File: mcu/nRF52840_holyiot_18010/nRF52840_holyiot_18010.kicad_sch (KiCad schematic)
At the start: 3 parts

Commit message: add reset module
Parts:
- removed MCU_SW1: SW_Push, ErgoCai.pretty:K2-1187SQ, symbol Switch:SW_Push
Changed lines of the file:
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@@
-		)
-	)
-	(wire
-		(pts
-			(xy 143.51 54.61) (xy 144.78 54.61)
-		)
-		(stroke
-			(width 0)
-			(type solid)
 		)
 	)
@@
 		(property "Intersheetrefs" "${INTERSHEET_REFS}"
 			(at 90.17 97.6303 90)
-			(effects
-				(font
-					(size 1.27 1.27)
-				)
-				(justify right)
-				(hide yes)
-			)
-		)
-	)
-	(global_label "RESET"
-		(shape input)
-		(at 143.51 54.61 180)
-		(fields_autoplaced yes)
-		(effects
-			(font
-				(size 1.27 1.27)
-			)
-			(justify right)
-		)
-		(property "Intersheetrefs" "${INTERSHEET_REFS}"
-			(at 134.7797 54.61 0)
 			(effects
 				(font
@@
 					(unit 1)
 				)
-			)
-		)
-	)
-	(symbol
-		(lib_id "power:GND")
-		(at 154.94 54.61 90)
-		(unit 1)
-		(exclude_from_sim no)
-		(in_bom yes)
-		(on_board yes)
-		(dnp no)
-		(property "Reference" "#PWR0103"
-			(at 161.29 54.61 0)
-			(effects
-				(font
-					(size 1.27 1.27)
-				)
-				(hide yes)
-			)
-		)
-		(property "Value" "GND"
-			(at 158.75 54.61 0)
-			(effects
-				(font
-					(size 1.27 1.27)
-				)
-			)
-		)
-		(property "Footprint" ""
-			(at 154.94 54.61 0)
-			(effects
-				(font
-					(size 1.27 1.27)
-				)
-				(hide yes)
-			)
-		)
-		(property "Datasheet" ""
-			(at 154.94 54.61 0)
-			(effects
-				(font
-					(size 1.27 1.27)
-				)
-				(hide yes)
-			)
-		)
-		(property "Description" "Power symbol creates a global label with name \"GND\" , ground"
-			(at 154.94 54.61 0)
-			(effects
-				(font
-					(size 1.27 1.27)
-				)
-				(hide yes)
-			)
-		)
-		(pin "1"
-		)
-		(instances
-			(project "nRF52840_holyiot_18010"
-				(path "/a75e1a70-312e-4b3d-9ad5-017ab62e82c1"
-					(reference "#PWR0103")
-					(unit 1)
-				)
-			)
-		)
-	)
-	(symbol
-		(lib_id "Switch:SW_Push")
-		(at 149.86 54.61 0)
-		(unit 1)
-		(exclude_from_sim no)
-		(in_bom yes)
-		(on_board yes)
-		(dnp no)
-		(property "Reference" "MCU_SW1"
-			(at 149.86 47.625 0)
-			(effects
-				(font
-					(size 1.27 1.27)
-				)
-			)
-		)
-		(property "Value" "SW_Push"
-			(at 149.86 50.165 0)
-			(effects
-				(font
-					(size 1.27 1.27)
-				)
-			)
-		)
-		(property "Footprint" "ErgoCai.pretty:K2-1187SQ"
-			(at 149.86 49.53 0)
-			(effects
-				(font
-					(size 1.27 1.27)
-				)
-				(hide yes)
-			)
-		)
-		(property "Datasheet" "~"
-			(at 149.86 49.53 0)
-			(effects
-				(font
-					(size 1.27 1.27)
-				)
-				(hide yes)
-			)
-		)
-		(property "Description" "Push button switch, generic, two pins"
-			(at 149.86 54.61 0)
-			(effects
-				(font
-					(size 1.27 1.27)
-				)
-				(hide yes)
-			)
-		)
-		(pin "1"
-		)
-		(pin "2"
-		)
-		(instances
-			(project "nRF52840_holyiot_18010"
-				(path "/a75e1a70-312e-4b3d-9ad5-017ab62e82c1"
-					(reference "MCU_SW1")
-					(unit 1)
-				)

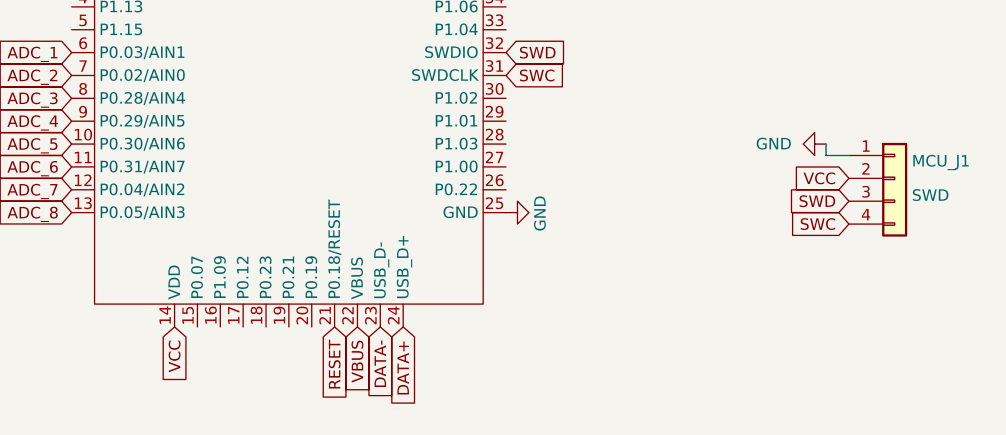
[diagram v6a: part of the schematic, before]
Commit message: update to 3.3V tag
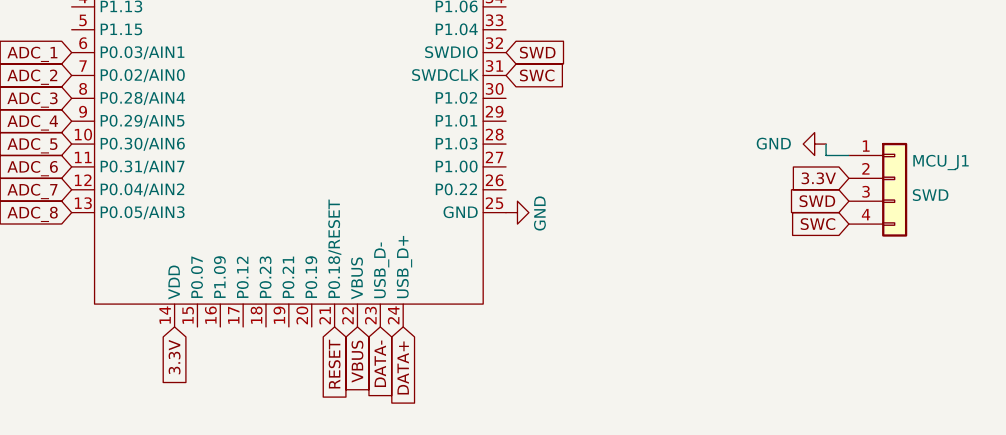
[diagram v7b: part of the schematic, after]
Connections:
- net VCC renamed 3.3V
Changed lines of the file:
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@@
 		)
 	)
-	(global_label "VCC"
+	(global_label "3.3V"
 		(shape input)
 		(at 147.32 72.39 180)
@@
 		)
 		(property "Intersheetrefs" "${INTERSHEET_REFS}"
-			(at 140.7062 72.39 0)
+			(at 140.2224 72.39 0)
 			(effects
 				(font
@@
 		)
 	)
-	(global_label "VCC"
+	(global_label "3.3V"
 		(shape input)
 		(at 72.39 88.9 270)
@@
 		)
 		(property "Intersheetrefs" "${INTERSHEET_REFS}"
-			(at 72.39 95.5138 90)
+			(at 72.39 95.9976 90)
 			(effects
 				(font
